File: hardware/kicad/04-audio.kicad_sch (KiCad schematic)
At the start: 9 parts, among them U5 PAM8403

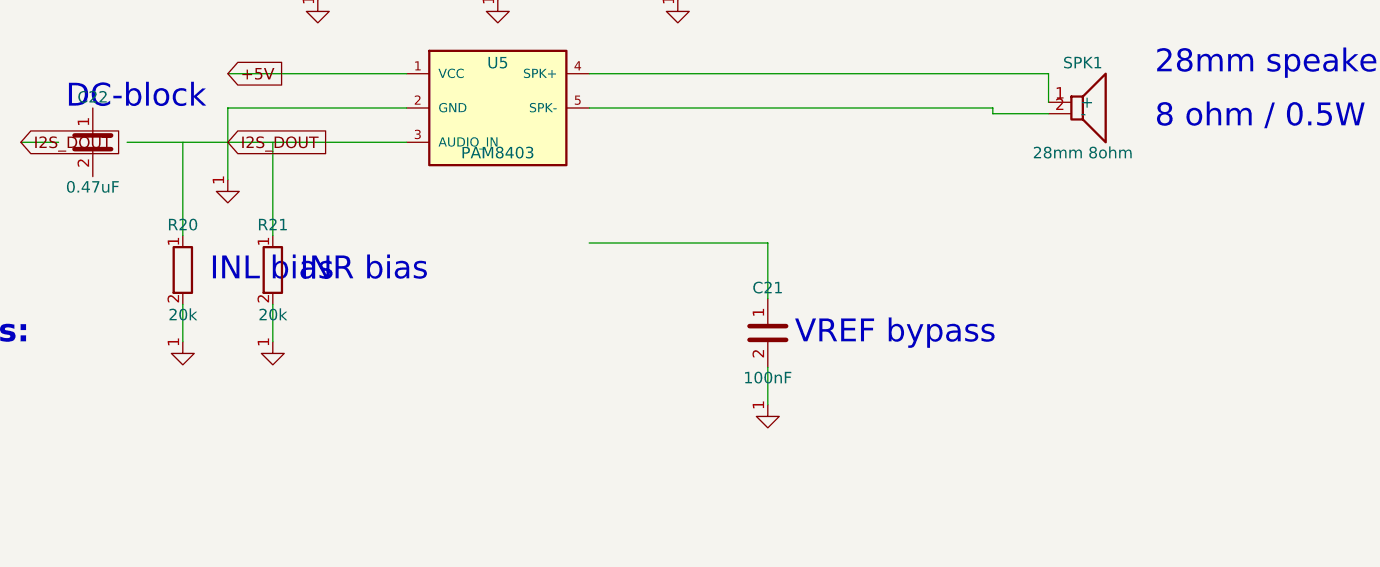
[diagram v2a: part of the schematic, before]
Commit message: fix(hw): R4 audit — schematic↔PCB sync guard + 4 fixes + R4-CRIT-1 false-positive closure
Round 4 of the hardware audit found four real schematic/PCB drift bugs
that rounds 1-3 missed because no check cross-validated the two Python
generators. A fifth finding (R4-CRIT-1, "FPC pinout mismatch") turned
out to be a FALSE POSITIVE caused by the landscape FPC pin reversal
(connector_pad = 41 − panel_pin) — verified programmatically against
all 40 J4 pads of the panel datasheet in components.md.

Fixes applied:
  R4-HIGH-1  USBLC6 (U4) + R22/R23 instantiated in power_supply.py —
             previously only in routing.py, invisible to schematic
             review.
  R4-HIGH-2  Display module symbol ref renamed U4 → DS1 in display.py.
             U4 is now cleanly owned by the physical USBLC6 TVS.
  R4-HIGH-3  PAM8403 R20/R21 input bias moved from GND to VREF
             (pin 8) per the datasheet single-ended app circuit.
  R4-CRIT-1  CLOSED as false positive. Both display.py (panel-side)
             and datasheet_specs.py (connector-side) were correct all
             along. Added 41-N reversal documentation at the top of
             both files so the mistake can't be re-raised.
  ERC CRIT   Pre-existing "Power output ↔ Power output" on +5V was
             PWR_FLAG duplicating IP5306 VOUT (already power_out in the
             library symbol). Removed the PWR_FLAG. ERC now 0 critical.

Incidental cleanups required by the new sync guard:
  - mcu.py R3 (external EN pull-up) removed from schematic — already
    DNP in BOM because the WROOM-1 module has an internal pull-up.
  - controls.py D1 BAT54C (MENU combo diode) instantiated in schematic
    to match the PCB routing. MENU button wiring simplified to the
    MENU_K node; there is no dedicated BTN_MENU GPIO (firmware detects
    START+SELECT combo).
  - power_supply.py USB_CC1 / USB_CC2 global labels added so the
    connector-net coverage check sees the full USB-C net set.
  - display.py docstring expanded with the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
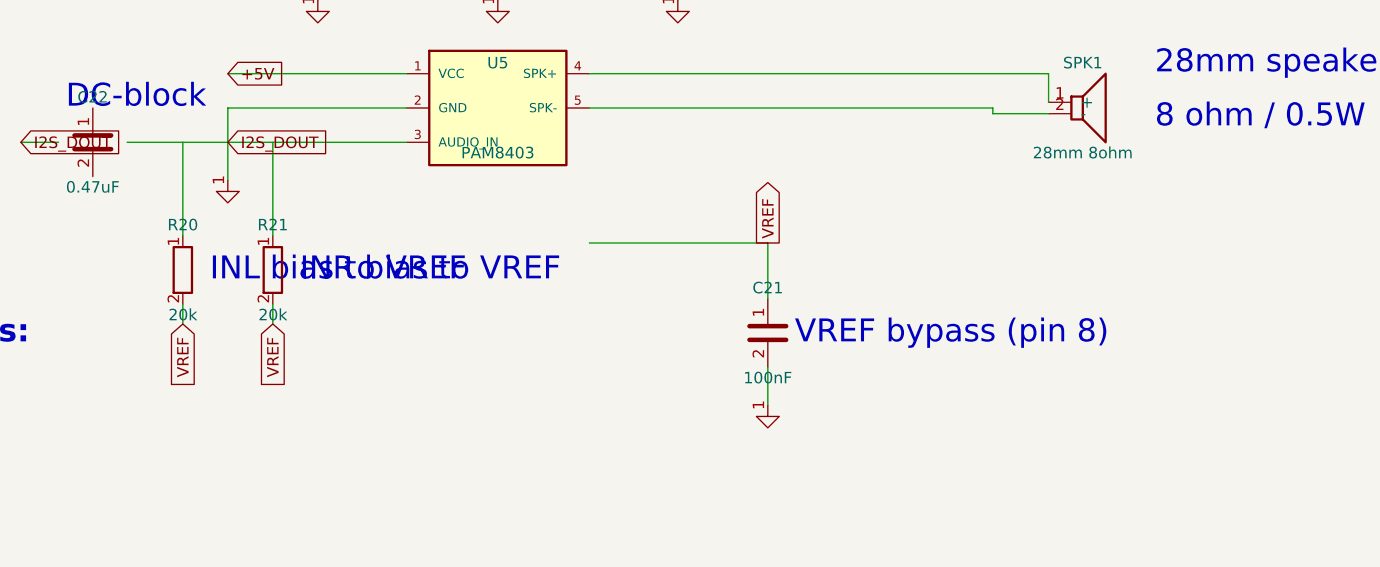
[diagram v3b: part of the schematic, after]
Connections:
- net VREF: now reaches C21.1
- net VREF: now also R20.2, R21.2
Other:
- note added: "INL bias to VREF"
- note added: "INR bias to VREF"
- note added: "VREF bypass (pin 8)"
- note removed: "INL bias"
- note removed: "INR bias"
- note removed: "VREF bypass"
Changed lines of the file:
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@@
   (symbol (lib_id "GND") (at 150 143 0) (unit 1) (exclude_from_sim no) (in_bom no) (on_board no) (dnp no) (property "Reference" "#PWR002" (at 150 141 0) (effects (font (size 1.27 1.27)) hide)) (property "Value" "GND" (at 150 145 0) (effects (font (size 1.27 1.27)) hide)) (pin "1"))
   (wire (pts (xy 150 138.81) (xy 150 143)) (stroke (width 0) (type default)))
-  (text "VREF bypass" (at 153 135 0) (effects (font (size 2.54 2.54)) (justify left)))
+  (global_label "VREF" (shape output) (at 150 125 90) (effects (font (size 1.27 1.27))) (property "Intersheetrefs" "" (at 0 0 0) (effects (font (size 1.27 1.27)) hide)))
+  (text "VREF bypass (pin 8)" (at 153 135 0) (effects (font (size 2.54 2.54)) (justify left)))
   (symbol (lib_id "C") (at 75 113.81 0) (unit 1) (exclude_from_sim no) (in_bom yes) (on_board yes) (dnp no) (property "Reference" "C22" (at 75 108.81 0) (effects (font (size 1.27 1.27)))) (property "Value" "0.47uF" (at 75 118.81 0) (effects (font (size 1.27 1.27)))) (pin "1") (pin "2"))
   (wire (pts (xy 78.81 113.81) (xy 90 113.81)) (stroke (width 0) (type default)))
@@
   (symbol (lib_id "R") (at 85 128 0) (unit 1) (exclude_from_sim no) (in_bom yes) (on_board yes) (dnp no) (property "Reference" "R20" (at 85 123 0) (effects (font (size 1.27 1.27)))) (property "Value" "20k" (at 85 133 0) (effects (font (size 1.27 1.27)))) (pin "1") (pin "2"))
   (wire (pts (xy 85 124.19) (xy 85 113.81)) (stroke (width 0) (type default)))
-  (symbol (lib_id "GND") (at 85 136 0) (unit 1) (exclude_from_sim no) (in_bom no) (on_board no) (dnp no) (property "Reference" "#PWR003" (at 85 134 0) (effects (font (size 1.27 1.27)) hide)) (property "Value" "GND" (at 85 138 0) (effects (font (size 1.27 1.27)) hide)) (pin "1"))
-  (wire (pts (xy 85 131.81) (xy 85 136)) (stroke (width 0) (type default)))
-  (text "INL bias" (at 88 128 0) (effects (font (size 2.54 2.54)) (justify left)))
+  (wire (pts (xy 85 131.81) (xy 85 134)) (stroke (width 0) (type default)))
+  (global_label "VREF" (shape input) (at 85 134 270) (effects (font (size 1.27 1.27))) (property "Intersheetrefs" "" (at 0 0 0) (effects (font (size 1.27 1.27)) hide)))
+  (text "INL bias to VREF" (at 88 128 0) (effects (font (size 2.54 2.54)) (justify left)))
   (symbol (lib_id "R") (at 95 128 0) (unit 1) (exclude_from_sim no) (in_bom yes) (on_board yes) (dnp no) (property "Reference" "R21" (at 95 123 0) (effects (font (size 1.27 1.27)))) (property "Value" "20k" (at 95 133 0) (effects (font (size 1.27 1.27)))) (pin "1") (pin "2"))
   (wire (pts (xy 95 124.19) (xy 95 113.81)) (stroke (width 0) (type default)))
-  (symbol (lib_id "GND") (at 95 136 0) (unit 1) (exclude_from_sim no) (in_bom no) (on_board no) (dnp no) (property "Reference" "#PWR004" (at 95 134 0) (effects (font (size 1.27 1.27)) hide)) (property "Value" "GND" (at 95 138 0) (effects (font (size 1.27 1.27)) hide)) (pin "1"))
-  (wire (pts (xy 95 131.81) (xy 95 136)) (stroke (width 0) (type default)))
-  (text "INR bias" (at 98 128 0) (effects (font (size 2.54 2.54)) (justify left)))
+  (wire (pts (xy 95 131.81) (xy 95 134)) (stroke (width 0) (type default)))
+  (global_label "VREF" (shape input) (at 95 134 270) (effects (font (size 1.27 1.27))) (property "Intersheetrefs" "" (at 0 0 0) (effects (font (size 1.27 1.27)) hide)))
+  (text "INR bias to VREF" (at 98 128 0) (effects (font (size 2.54 2.54)) (justify left)))
   (symbol (lib_id "C") (at 100 90 0) (unit 1) (exclude_from_sim no) (in_bom yes) (on_board yes) (dnp no) (property "Reference" "C23" (at 100 85 0) (effects (font (size 1.27 1.27)))) (property "Value" "1uF" (at 100 95 0) (effects (font (size 1.27 1.27)))) (pin "1") (pin "2"))
   (global_label "+5V" (shape input) (at 100 82 0) (effects (font (size 1.27 1.27))) (property "Intersheetrefs" "" (at 0 0 0) (effects (font (size 1.27 1.27)) hide)))
   (wire (pts (xy 100 86.19) (xy 100 82)) (stroke (width 0) (type default)))
-  (symbol (lib_id "GND") (at 100 98 0) (unit 1) (exclude_from_sim no) (in_bom no) (on_board no) (dnp no) (property "Reference" "#PWR005" (at 100 96 0) (effects (font (size 1.27 1.27)) hide)) (property "Value" "GND" (at 100 100 0) (effects (font (size 1.27 1.27)) hide)) (pin "1"))
+  (symbol (lib_id "GND") (at 100 98 0) (unit 1) (exclude_from_sim no) (in_bom no) (on_board no) (dnp no) (property "Reference" "#PWR003" (at 100 96 0) (effects (font (size 1.27 1.27)) hide)) (property "Value" "GND" (at 100 100 0) (effects (font (size 1.27 1.27)) hide)) (pin "1"))
   (wire (pts (xy 100 93.81) (xy 100 98)) (stroke (width 0) (type default)))
   (text "VDD decoupl." (at 103 90 0) (effects (font (size 2.54 2.54)) (justify left)))
@@
   (global_label "+5V" (shape input) (at 120 82 0) (effects (font (size 1.27 1.27))) (property "Intersheetrefs" "" (at 0 0 0) (effects (font (size 1.27 1.27)) hide)))
   (wire (pts (xy 120 86.19) (xy 120 82)) (stroke (width 0) (type default)))
-  (symbol (lib_id "GND") (at 120 98 0) (unit 1) (exclude_from_sim no) (in_bom no) (on_board no) (dnp no) (property "Reference" "#PWR006" (at 120 96 0) (effects (font (size 1.27 1.27)) hide)) (property "Value" "GND" (at 120 100 0) (effects (font (size 1.27 1.27)) hide)) (pin "1"))
+  (symbol (lib_id "GND") (at 120 98 0) (unit 1) (exclude_from_sim no) (in_bom no) (on_board no) (dnp no) (property "Reference" "#PWR004" (at 120 96 0) (effects (font (size 1.27 1.27)) hide)) (property "Value" "GND" (at 120 100 0) (effects (font (size 1.27 1.27)) hide)) (pin "1"))
   (wire (pts (xy 120 93.81) (xy 120 98)) (stroke (width 0) (type default)))
   (text "PVDD top" (at 123 90 0) (effects (font (size 2.54 2.54)) (justify left)))
@@
   (global_label "+5V" (shape input) (at 140 82 0) (effects (font (size 1.27 1.27))) (property "Intersheetrefs" "" (at 0 0 0) (effects (font (size 1.27 1.27)) hide)))
   (wire (pts (xy 140 86.19) (xy 140 82)) (stroke (width 0) (type default)))
-  (symbol (lib_id "GND") (at 140 98 0) (unit 1) (exclude_from_sim no) (in_bom no) (on_board no) (dnp no) (property "Reference" "#PWR007" (at 140 96 0) (effects (font (size 1.27 1.27)) hide)) (property "Value" "GND" (at 140 100 0) (effects (font (size 1.27 1.27)) hide)) (pin "1"))
+  (symbol (lib_id "GND") (at 140 98 0) (unit 1) (exclude_from_sim no) (in_bom no) (on_board no) (dnp no) (property "Reference" "#PWR005" (at 140 96 0) (effects (font (size 1.27 1.27)) hide)) (property "Value" "GND" (at 140 100 0) (effects (font (size 1.27 1.27)) hide)) (pin "1"))
   (wire (pts (xy 140 93.81) (xy 140 98)) (stroke (width 0) (type default)))
   (text "PVDD bottom" (at 143 90 0) (effects (font (size 2.54 2.54)) (justify left)))

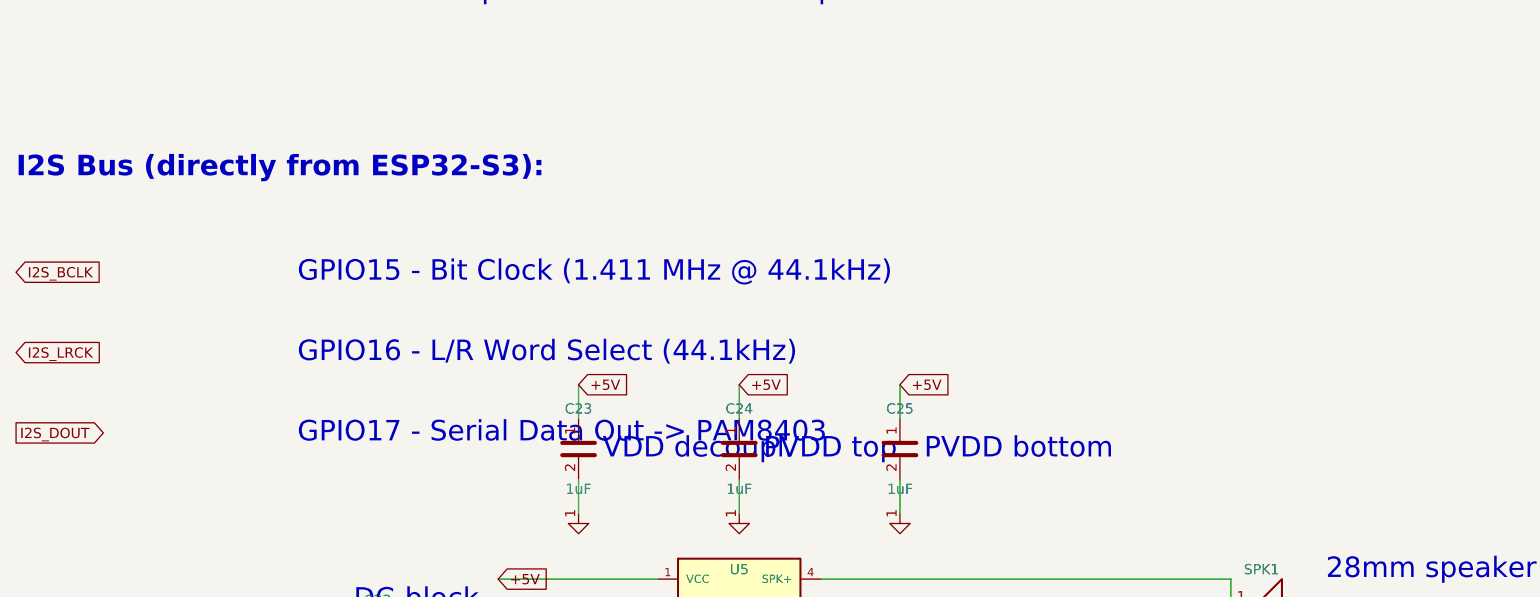
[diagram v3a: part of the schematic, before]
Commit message: docs(R10): close 8 LOW-severity doc-drift findings from Layer 2 audit
Round 10 hardware-audit Layer 2 prose pass found no functional bugs
(0 CRIT/HIGH/MED) but surfaced 8 stale comments and doc-drift items
across schematic generator text labels, datasheet_specs.py function
strings, verify_strapping_pins.py RC timing math, and
snes-optimization.md. All fixed in this single commit — no PCB
regeneration, no routing/geometry changes.

- R10-LOW-1: mcu.py GPIO table labeled "GPIO26-32 = Octal PSRAM" but
  those are actually Octal Flash pins on ESP32-S3-WROOM-1 N16R8.
  PSRAM is on GPIO33-37. Relabeled to show both Flash and PSRAM.

- R10-LOW-2: audio.py I2S bus reference text said "BCLK 1.411MHz @
  44.1kHz" but firmware uses PDM TX (no BCLK/LRCK) at 32kHz.
  Relabeled GPIO15/16 as UNUSED with a v2-reuse note (candidates for
  ADC2 battery voltage). Dead-net removal deferred to v2 respin.

- R10-LOW-3: sd_card.py said "SPI @ up to 40MHz" but firmware runs
  20MHz (R2-MED-5 trace-length cap). Updated design-note text.

- R10-LOW-4: sd_card.py said "GPIO36-39 grouped for clean SPI" but
  actual SPI pins are GPIO38/39 (CLK/CS) + GPIO43/44 (MISO/MOSI) —
  split across the WROOM-1 module. Updated design-note text.

- R10-LOW-5: datasheet_specs.py J4 pads 15/16 function strings said
  "NC (IM0/IM1 mode select)" but after the 41-N panel pin reversal
  those pads correspond to DB9/DB8 (unused upper data bits in 8-bit
  8080 mode). IM0/IM1 are actually on J4 pads 3/2. Fixed function
  strings with a comment explaining the 41-N mapping.

- R10-LOW-6: datasheet_specs.py U5 block comment said "left channel
  only: OUTL+ → SPK+, OUTL- → SPK-" but the pad map wires SPK± to
  OUTR+/OUTR- (pins 14/16). OUTL+/- are floating. Rewrote the
  comment + pin 1/3 function strings to match the actual wiring.

- R10-LOW-7: verify_strapping_pins.py test_en_rc_delay() computed
  tau = 10kΩ·100nF = 1ms assuming external R3, but R4 closed R3 as
  DNP and the WROOM-1 module integrates a ~45kΩ EN pull-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
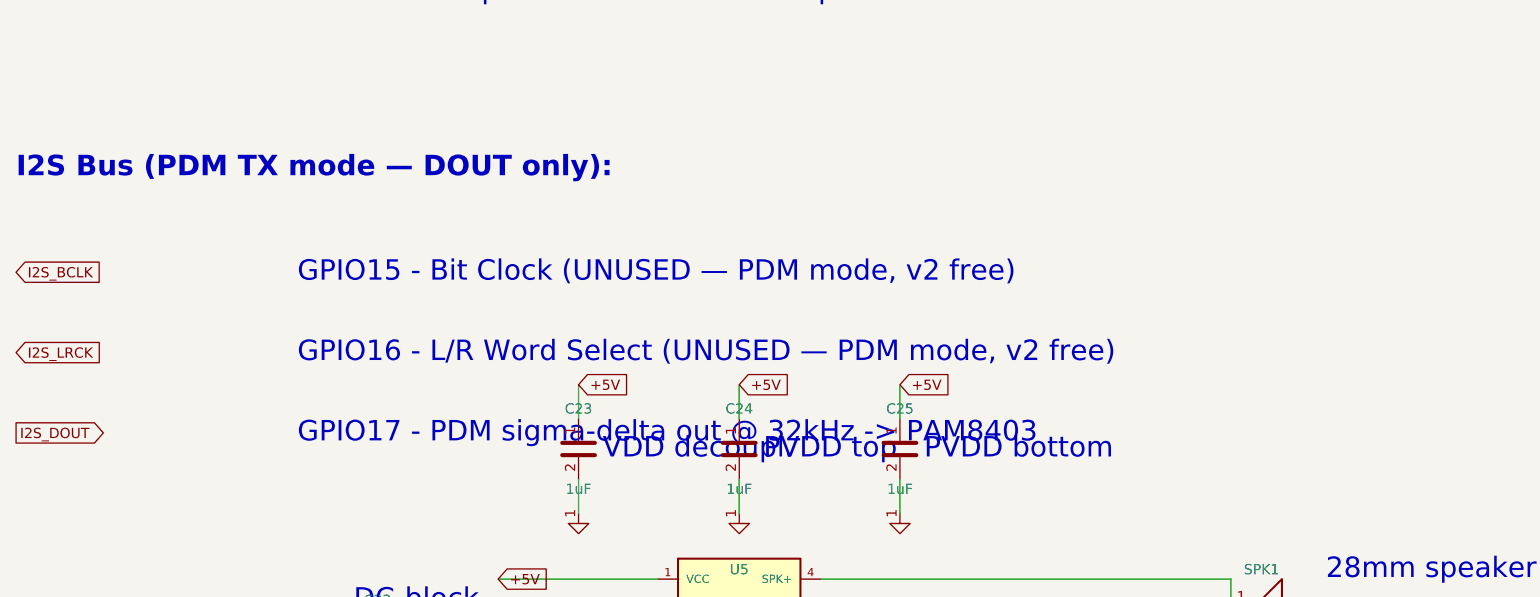
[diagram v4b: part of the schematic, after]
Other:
- note added: "GPIO15 - Bit Clock (UNUSED — PDM mode, v2 free)"
- note added: "GPIO16 - L/R Word Select (UNUSED — PDM mode, v2 free)"
- note added: "GPIO17 - PDM sigma-delta out @ 32kHz -> PAM8403"
- note added: "I2S Bus (PDM TX mode — DOUT only):"
- note removed: "GPIO15 - Bit Clock (1.411 MHz @ 44.1kHz)"
- note removed: "GPIO16 - L/R Word Select (44.1kHz)"
- note removed: "GPIO17 - Serial Data Out -> PAM8403"
- note removed: "I2S Bus (directly from ESP32-S3):"
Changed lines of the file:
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@@
   (global_label "I2S_DOUT" (shape input) (at 90 113.81 0) (effects (font (size 1.27 1.27))) (property "Intersheetrefs" "" (at 0 0 0) (effects (font (size 1.27 1.27)) hide)))
   (wire (pts (xy 90 113.81) (xy 109.84 113.81)) (stroke (width 0) (type default)))
-  (text "I2S Bus (directly from ESP32-S3):" (at 30 55 0) (effects (font (size 2.54 2.54) bold) (justify left)))
+  (text "I2S Bus (PDM TX mode — DOUT only):" (at 30 55 0) (effects (font (size 2.54 2.54) bold) (justify left)))
   (global_label "I2S_BCLK" (shape input) (at 30 68 0) (effects (font (size 1.27 1.27))) (property "Intersheetrefs" "" (at 0 0 0) (effects (font (size 1.27 1.27)) hide)))
-  (text "GPIO15 - Bit Clock (1.411 MHz @ 44.1kHz)" (at 65 68 0) (effects (font (size 2.54 2.54)) (justify left)))
+  (text "GPIO15 - Bit Clock (UNUSED — PDM mode, v2 free)" (at 65 68 0) (effects (font (size 2.54 2.54)) (justify left)))
   (global_label "I2S_LRCK" (shape input) (at 30 78 0) (effects (font (size 1.27 1.27))) (property "Intersheetrefs" "" (at 0 0 0) (effects (font (size 1.27 1.27)) hide)))
-  (text "GPIO16 - L/R Word Select (44.1kHz)" (at 65 78 0) (effects (font (size 2.54 2.54)) (justify left)))
+  (text "GPIO16 - L/R Word Select (UNUSED — PDM mode, v2 free)" (at 65 78 0) (effects (font (size 2.54 2.54)) (justify left)))
   (global_label "I2S_DOUT" (shape output) (at 30 88 0) (effects (font (size 1.27 1.27))) (property "Intersheetrefs" "" (at 0 0 0) (effects (font (size 1.27 1.27)) hide)))
-  (text "GPIO17 - Serial Data Out -> PAM8403" (at 65 88 0) (effects (font (size 2.54 2.54)) (justify left)))
+  (text "GPIO17 - PDM sigma-delta out @ 32kHz -> PAM8403" (at 65 88 0) (effects (font (size 2.54 2.54)) (justify left)))
   (symbol (lib_id "Speaker") (at 185 110 0) (unit 1) (exclude_from_sim no) (in_bom yes) (on_board yes) (dnp no) (property "Reference" "SPK1" (at 185 105 0) (effects (font (size 1.27 1.27)))) (property "Value" "28mm 8ohm" (at 185 115 0) (effects (font (size 1.27 1.27)))) (pin "1") (pin "2"))
   (text "28mm speaker" (at 193 105 0) (effects (font (size 2.54 2.54)) (justify left)))
